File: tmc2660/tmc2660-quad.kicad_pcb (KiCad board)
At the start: 4 copper layers, 125 x 40 mm, 81 parts, among them J1 Power, J100 0R, J2 DataIn, J200 0R, J300 0R, J400 0R, M0 Mount, M1 Mount, M100 Mount, M101 Mount, M200 Mount, M201 Mount, M300 Mount, M301 Mount, M400 Mount, M401 Mount, P100 Motor, P200 Motor, P300 Motor, P400 Motor, U100 TMC2660, U200 TMC2660, U300 TMC2660, U400 TMC2660

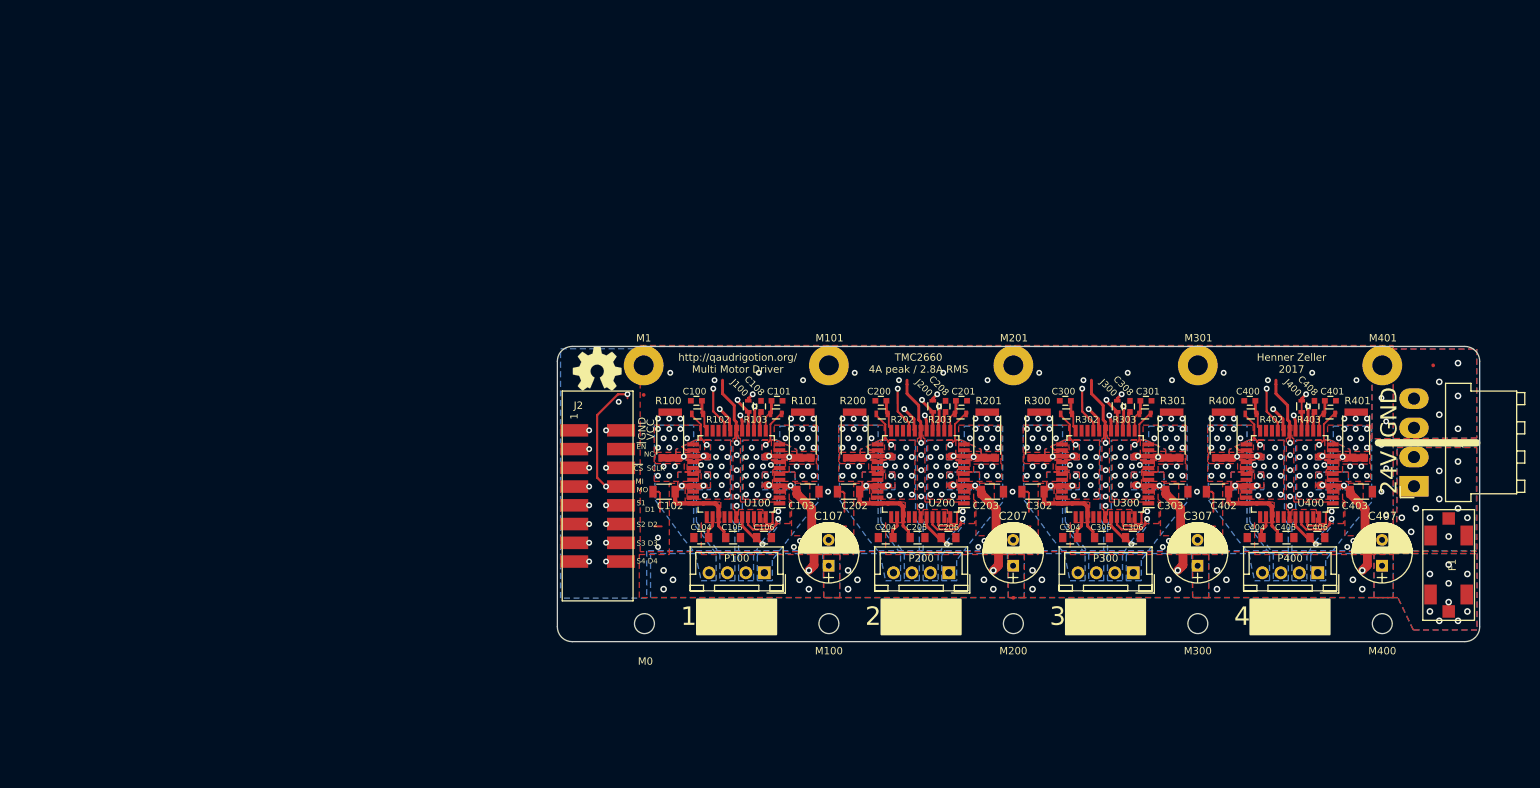
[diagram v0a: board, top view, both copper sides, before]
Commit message: Started work on moving to 100x50mm design
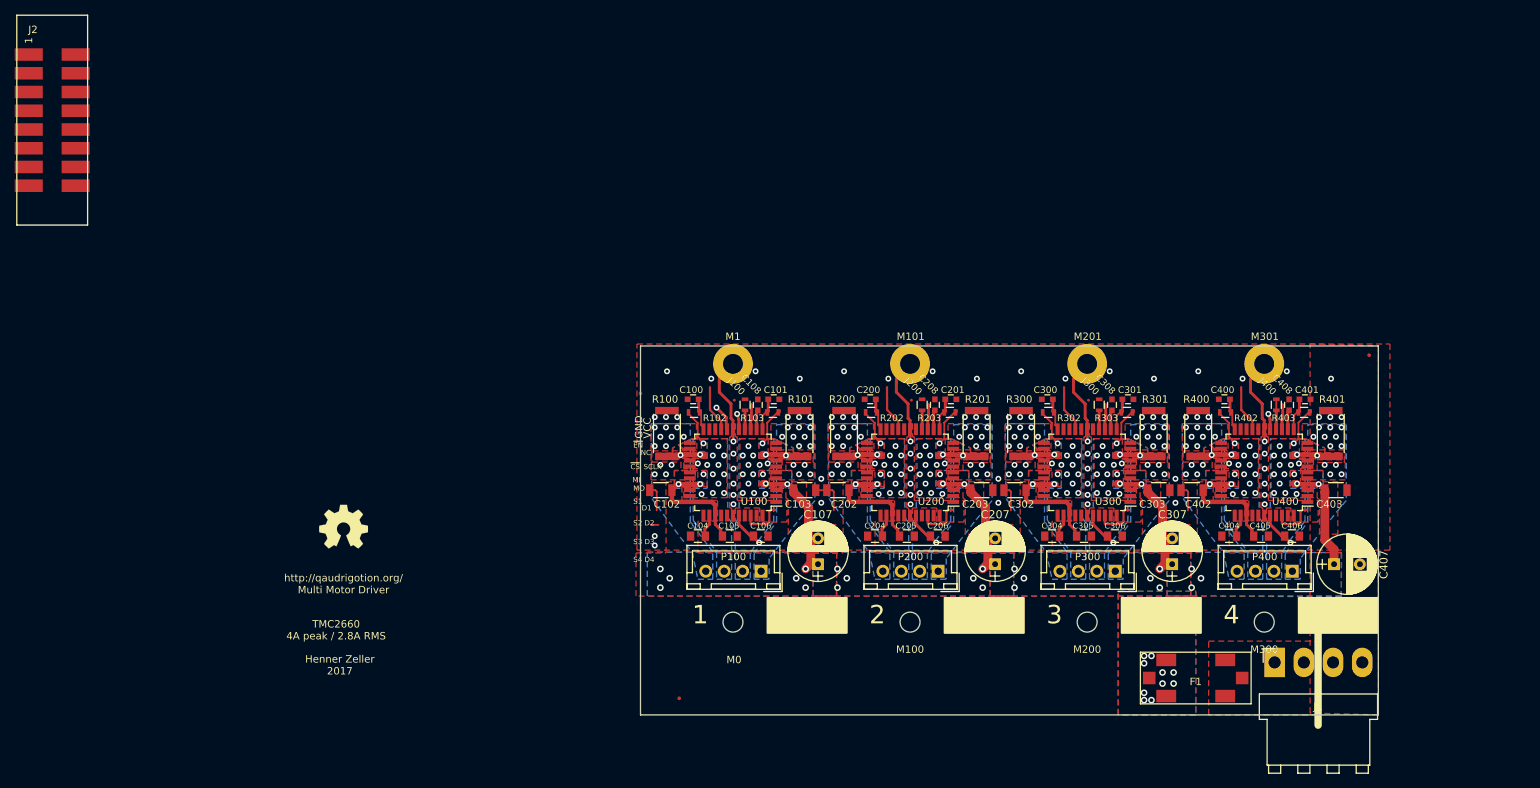
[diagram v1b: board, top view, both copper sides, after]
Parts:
- removed M400: Mount, Mounting_Holes:MountingHole_2.7mm_M2.5
- removed M401: Mount, Mounting_Holes:MountingHole_2.7mm_M2.5_Pad
- moved J2 89.8 mm to (18.5, 20.4)
- moved REF** 47.3 mm to (104.7, 107.6)
- moved REF*** 40.5 mm to (59.2, 84.4)
- moved F1 37.5 mm to (174.7, 104.9), turned to 0 degrees
- moved J1 30.4 mm to (185.4, 102.8), turned to 0 degrees
- moved M1 12.1 mm to (112.0, 62.3)
- moved M0 12.0 mm to (112.0, 97.3)
- moved M100 11.0 mm to (136.0, 97.3)
- moved M101 11.0 mm to (136.0, 62.3)
- moved M200 10.0 mm to (160.0, 97.3)
- moved M201 10.0 mm to (160.0, 62.3)
- moved M300 9.00 mm to (184.0, 97.3)
- moved M301 9.00 mm to (184.0, 62.3)
- moved REF** 8.79 mm to (198.2, 61.1)
- moved C407 6.51 mm to (193.5, 89.4), turned to 0 degrees
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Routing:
- net GLOBAL_MOSI: track 134.6 -> 4.07 mm, vias 6 -> 0
- net CS: track 126.8 -> 4.87 mm, vias 5 -> 1
- net DIR4: track 113.1 -> 0.00 mm, vias 2 -> 0
- net SCLK: track 122.8 -> 12.0 mm, vias 5 -> 2
- net ~ENABLE: track 135.6 -> 25.3 mm, vias 5 -> 0
- net STEP4: track 115.5 -> 6.13 mm, vias 2 -> 0
- net DIR3: track 85.9 -> 0.00 mm, vias 2 -> 0
- net STEP3: track 88.6 -> 6.13 mm, vias 2 -> 0
- net DIR2: track 59.3 -> 0.00 mm, vias 2 -> 0
- net STEP2: track 61.9 -> 6.13 mm, vias 2 -> 0
- net GLOBAL_MISO: track 38.0 -> 3.69 mm, vias 3 -> 0
- net DIR1: track 32.7 -> 0.00 mm, vias 2 -> 0
- net /TMC2660-400/MISO: track 36.2 -> 6.28 mm, vias 2 -> 0
- net /TMC2660-300/MISO: track 36.2 -> 6.28 mm, vias 2 -> 0
- net /TMC2660-200/MISO: track 36.2 -> 6.28 mm, vias 2 -> 0
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- removed copper zone on B.Cu, net /PowerIn
- removed copper zone on In1.Cu, net /PowerIn
- removed copper zone on In2.Cu, net /PowerIn
- removed copper zone on B.Cu, net GND
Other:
- board size 125 x 40 mm -> 100 x 50 mm

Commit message: Finished squished board
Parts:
- added D1: BAV70, TO_SOT_Packages_SMD:SOT-363_SC-70-6_Handsoldering, F.Cu at (111.0, 101.0)
- added J3: 10k, Resistors_SMD:R_0603, F.Cu at (108.6, 105.0)
- moved REF** 165.2 mm to (262.2, 57.9)
- moved J2 128.5 mm to (114.9, 105.3), turned to 0 degrees
- moved M0 1.00 mm to (112.0, 96.3)
- moved M100 1.00 mm to (136.0, 96.3)
- moved M200 1.00 mm to (160.0, 96.3)
- moved M300 1.00 mm to (184.0, 96.3)
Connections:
- J1 pad 4: GND -> Net-(J1-Pad4)
- J2 pad 4: Net-(J2-Pad4) -> STALL
- U100 pad 38: Net-(U100-Pad38) -> /TMC2660-100/STALL
- U200 pad 38: Net-(U200-Pad38) -> /TMC2660-200/STALL
- U300 pad 38: Net-(U300-Pad38) -> /TMC2660-300/STALL
- U400 pad 38: Net-(U400-Pad38) -> /TMC2660-400/STALL
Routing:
- net CS: track 4.87 -> 159.7 mm, vias 1 -> 5
- net GLOBAL_MOSI: track 4.07 -> 155.7 mm, vias 0 -> 5
- net DIR4: track 0.00 -> 142.5 mm, vias 0 -> 2
- net STEP4: track 6.13 -> 143.7 mm, vias 0 -> 2
- net SCLK: track 12.0 -> 147.9 mm, vias 2 -> 5
- net ~ENABLE: track 25.3 -> 148.2 mm, vias 0 -> 5
- net DIR3: track 0.00 -> 117.6 mm, vias 0 -> 2
- net STEP3: track 6.13 -> 118.6 mm, vias 0 -> 2
- net /TMC2660-400/STALL: track 0.00 -> 101.6 mm, vias 0 -> 2
- net DIR2: track 0.00 -> 92.3 mm, vias 0 -> 2
- net STEP2: track 6.13 -> 93.3 mm, vias 0 -> 2
- net GLOBAL_MISO: track 3.69 -> 87.9 mm, vias 0 -> 2
- net /TMC2660-300/STALL: track 0.00 -> 77.5 mm, vias 0 -> 2
- net DIR1: track 0.00 -> 67.9 mm, vias 0 -> 2
- net STEP1: track 6.13 -> 68.0 mm, vias 0 -> 2
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- added copper zone on B.Cu, net GND
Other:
- net class Default: clearance 0.21 -> 0.1778; trace_width 0.25 -> 0.200406
- rule trace_clearance: 0.21 -> 0.1778

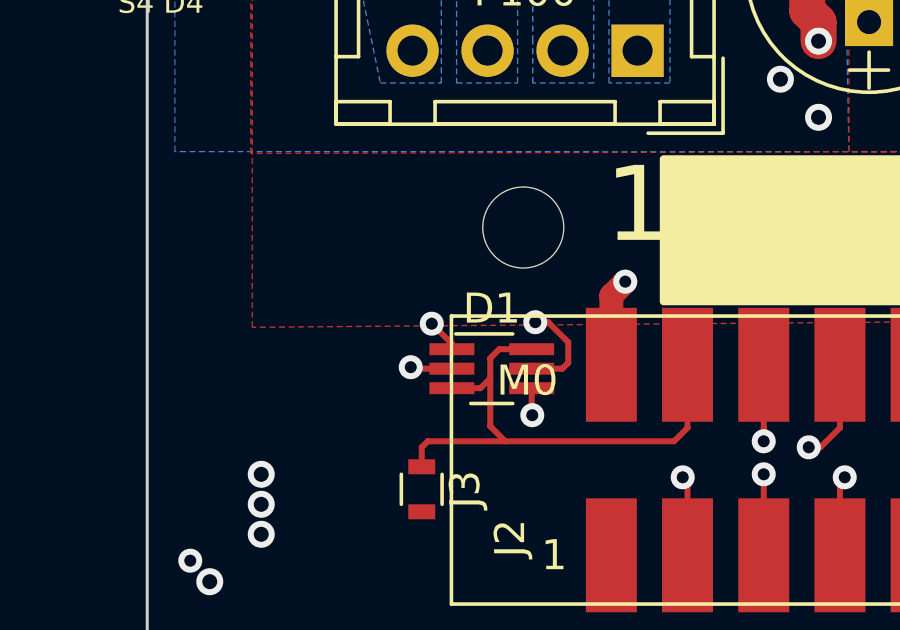
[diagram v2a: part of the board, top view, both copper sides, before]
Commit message: Fixed some mistakes pointed out
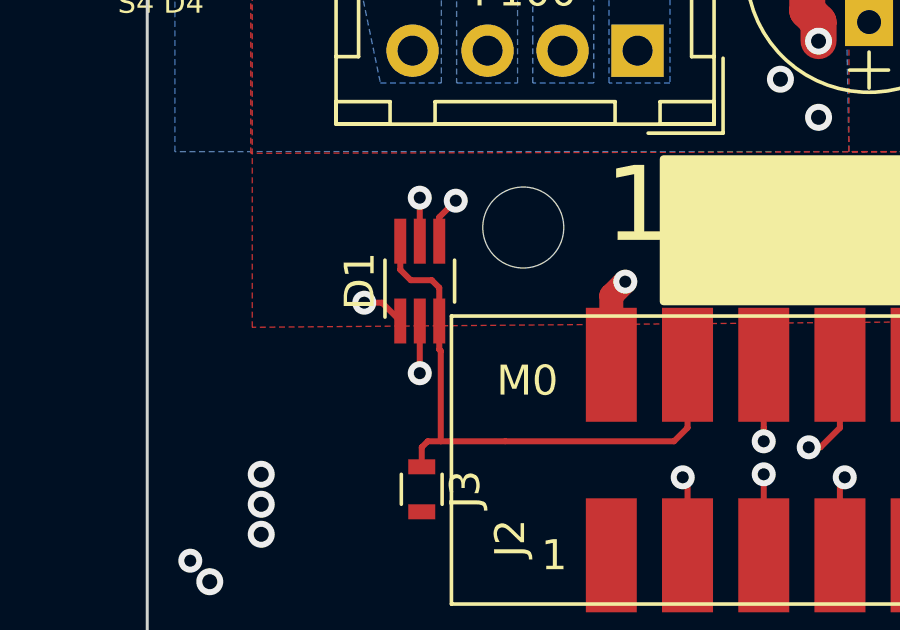
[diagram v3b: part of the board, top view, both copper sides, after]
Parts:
- moved D1 3.78 mm to (108.5, 98.1), turned to 90 degrees
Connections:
- J1 pad 4: Net-(J1-Pad4) -> GND
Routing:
- net /TMC2660-400/STALL: track 101.6 -> 92.1 mm
- net /TMC2660-300/STALL: track 77.5 -> 71.8 mm
- net /TMC2660-200/STALL: track 48.7 -> 46.8 mm
- net STALL: track 17.8 -> 19.5 mm
- net /TMC2660-100/STALL: track 24.9 -> 25.9 mm

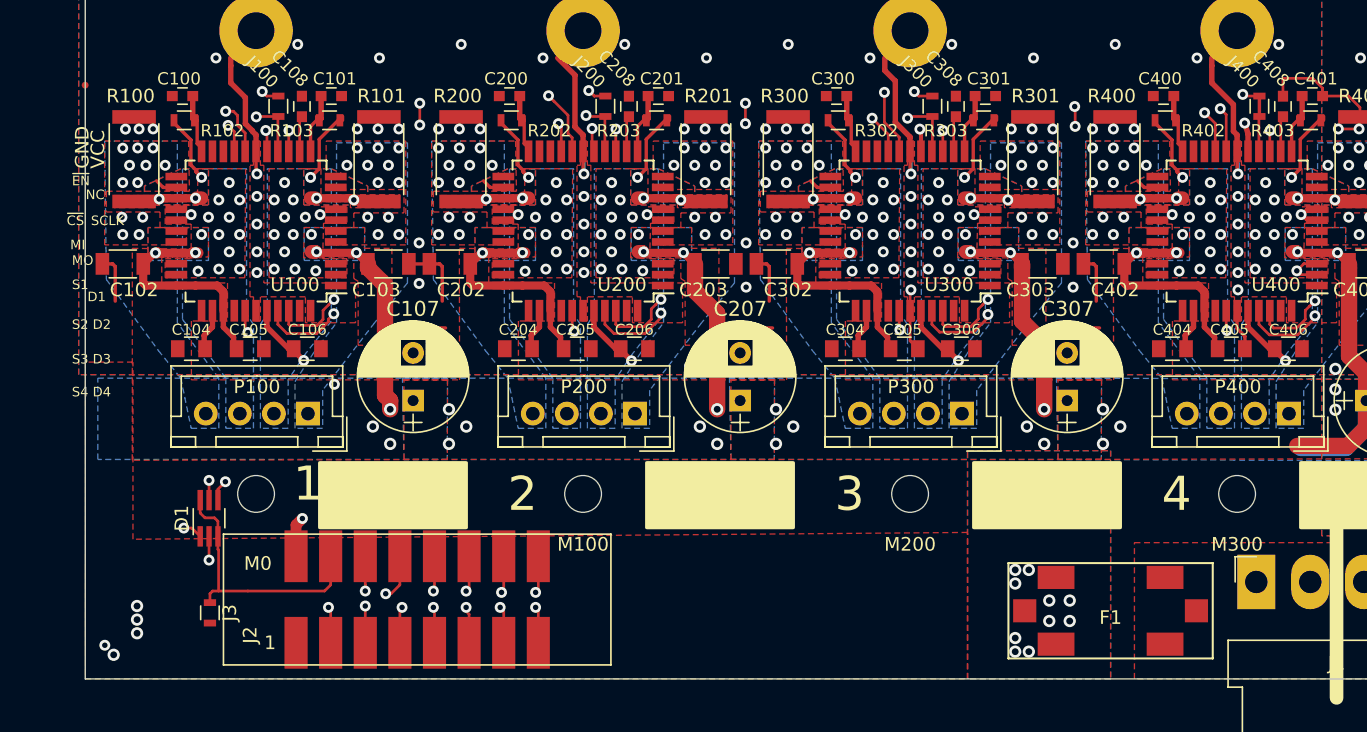
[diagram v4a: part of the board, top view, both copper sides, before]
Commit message: Further fixed broken gnd pour
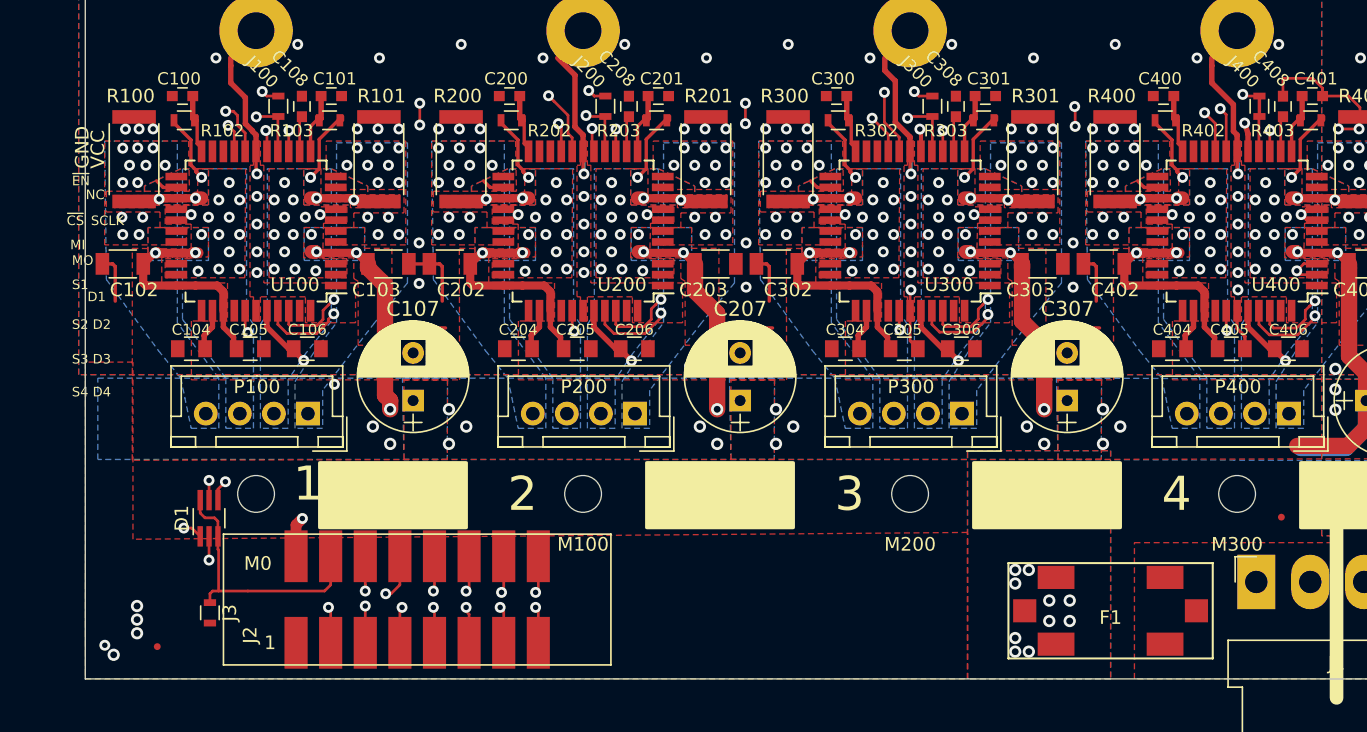
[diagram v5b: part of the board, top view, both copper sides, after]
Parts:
- added REF**: Fiducial_0.5mm_Dia_1mm_Outer, Fiducials:Fiducial_0.5mm_Dia_1mm_Outer, F.Cu at (187.2, 98.0)
- moved REF** 41.5 mm to (104.8, 107.5)
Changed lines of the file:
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@@
     (tracks 1401)
     (zones 0)
-    (modules 81)
+    (modules 82)
     (nets 70)
   )
   (page A4)
   (layers
-    (0 F.Cu signal)
+    (0 F.Cu signal hide)
     (1 In1.Cu signal)
-    (2 In2.Cu signal)
-    (31 B.Cu signal)
+    (2 In2.Cu signal hide)
+    (31 B.Cu signal hide)
     (32 B.Adhes user)
     (33 F.Adhes user)
     (34 B.Paste user)
     (35 F.Paste user)
-    (36 B.SilkS user)
+    (36 B.SilkS user hide)
     (37 F.SilkS user)
-    (38 B.Mask user)
-    (39 F.Mask user)
+    (38 B.Mask user hide)
+    (39 F.Mask user hide)
     (40 Dwgs.User user)
     (41 Cmts.User user hide)
@@
     (add_net VMot)
   )
+  (module Fiducials:Fiducial_0.5mm_Dia_1mm_Outer locked (layer F.Cu)
+    (at 187.25 98)
+    (descr "Circular Fiducial, 0.5mm bare copper top; 1mm keepout (Level C)")
+    (tags marker)
+    (attr virtual)
+    (fp_text reference REF** (at 0 -1.5) (layer F.SilkS) hide
+      (effects (font (size 1 1) (thickness 0.15)))
+    )
+    (fp_text value Fiducial_0.5mm_Dia_1mm_Outer (at 0 1.5) (layer F.Fab) hide
+      (effects (font (size 1 1) (thickness 0.15)))
+    )
+    (fp_circle (center 0 0) (end 0.5 0) (layer F.Fab) (width 0.1))
+    (fp_text user %R (at 0 0) (layer F.Fab)
+      (effects (font (size 0.2 0.2) (thickness 0.04)))
+    )
+    (fp_circle (center 0 0) (end 0.75 0) (layer F.CrtYd) (width 0.05))
+    (pad ~ smd circle (at 0 0) (size 0.5 0.5) (layers F.Cu F.Mask)
+      (solder_mask_margin 0.25) (clearance 0.25))
+  )
   (module TO_SOT_Packages_SMD:SOT-363_SC-70-6_Handsoldering (layer F.Cu)
     (at 108.55 98.08 90)
@@
   )
   (module Fiducials:Fiducial_0.5mm_Dia_1mm_Outer locked (layer F.Cu)
-    (at 99.4575 66.294)
+    (at 104.75 107.5)
     (descr "Circular Fiducial, 0.5mm bare copper top; 1mm keepout (Level C)")
     (tags marker)
@@
     (polygon
       (pts
-        (xy 123.7475 79.794) (xy 118.1595 79.794) (xy 118.1595 70.396) (xy 123.7475 70.396)
+        (xy 123.7475 79.794) (xy 118.1595 79.794) (xy 118.1595 70.396) (xy 122.75 70.4) (xy 123.75 71.4)
       )
     )
@@
     (polygon
       (pts
-        (xy 147.7475 79.794) (xy 142.1595 79.794) (xy 142.1595 70.396) (xy 147.7475 70.396)
+        (xy 147.7 71.4) (xy 147.7475 79.794) (xy 142.1595 79.794) (xy 142.1595 70.396) (xy 146.7 70.4)
       )
     )
@@
     (polygon
       (pts
-        (xy 129.7135 79.794) (xy 124.189 79.794) (xy 124.189 70.396) (xy 129.7135 70.396)
+        (xy 129.7135 79.794) (xy 124.189 79.794) (xy 124.2 71.4) (xy 125.2 70.4) (xy 129.7135 70.396)
       )
     )
@@
     (polygon
       (pts
-        (xy 171.7475 79.794) (xy 166.1595 79.794) (xy 166.1595 70.396) (xy 171.7475 70.396)
+        (xy 171.7475 79.794) (xy 166.1595 79.794) (xy 166.1595 70.396) (xy 170.75 70.4) (xy 171.75 71.4)
       )
     )
@@
     (polygon
       (pts
-        (xy 153.7135 79.794) (xy 148.189 79.794) (xy 148.189 70.396) (xy 153.7135 70.396)
+        (xy 153.7135 79.794) (xy 148.189 79.794) (xy 148.2 71.4) (xy 149.2 70.4) (xy 153.1 70.4)
+        (xy 153.7 71)
       )
     )
@@
     (polygon
       (pts
-        (xy 177.7135 79.794) (xy 172.189 79.794) (xy 172.189 70.396) (xy 177.7135 70.396)
+        (xy 177.7135 79.794) (xy 172.189 79.794) (xy 172.1945 75.597) (xy 172.2 71.4) (xy 173.2 70.4)
+        (xy 177.7135 70.396)
       )
     )
@@
     )
   )
-  (zone (net 0) (net_name "") (layer F.Mask) (hatch edge 0.508)
+  (zone (net 0) (net_name "") (layers F&B.Cu) (hatch edge 0.508)
     (connect_pads (clearance 0.254))
     (min_thickness 0.254)
-    (fill yes (arc_segments 16) (thermal_gap 0.508) (thermal_bridge_width 0.508))
+    (keepout (tracks not_allowed) (vias not_allowed) (copperpour not_allowed))
+    (fill (arc_segments 16) (thermal_gap 0.508) (thermal_bridge_width 0.508))
     (polygon
       (pts
-        (xy 107.75 101) (xy 107.75 105) (xy 104 105) (xy 104 101)
+        (xy 104 103) (xy 104 100.5) (xy 107.75 100.5) (xy 107.75 105) (xy 106 105)
       )
     )
   )
-  (zone (net 0) (net_name "") (layers F&B.Cu) (hatch edge 0.508)
+  (zone (net 0) (net_name "") (layer B.Mask) (hatch edge 0.508)
     (connect_pads (clearance 0.254))
     (min_thickness 0.254)
-    (keepout (tracks not_allowed) (vias not_allowed) (copperpour not_allowed))
-    (fill (arc_segments 16) (thermal_gap 0.508) (thermal_bridge_width 0.508))
+    (fill yes (arc_segments 16) (thermal_gap 0.508) (thermal_bridge_width 0.508))
     (polygon
       (pts
-        (xy 104 101) (xy 107.75 101) (xy 107.75 105) (xy 104 105)
+        (xy 107.75 100.5) (xy 107.75 105) (xy 106 105) (xy 104 103) (xy 104 100.5)
       )
     )
   )
-  (zone (net 0) (net_name "") (layer B.Mask) (hatch edge 0.508)
+  (zone (net 0) (net_name "") (layer F.Mask) (hatch edge 0.508)
     (connect_pads (clearance 0.254))
     (min_thickness 0.254)
@@
     (polygon
       (pts
-        (xy 107.75 101) (xy 107.75 105) (xy 104 105) (xy 104 101)
+        (xy 107.75 100.5) (xy 107.75 105) (xy 106 105) (xy 104 103) (xy 104 100.5)
       )
     )

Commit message: Commiting before branching
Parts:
- added G***: LOGO, graphics:kiwi, F.Cu at (153.2, 104.5)
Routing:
- net GND: vias 84 -> 92
